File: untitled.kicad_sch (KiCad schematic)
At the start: 12 parts, among them Q1 AO3401A, U2 STM32L100RBT6A_LQFP64, U4 RC1587_3V3

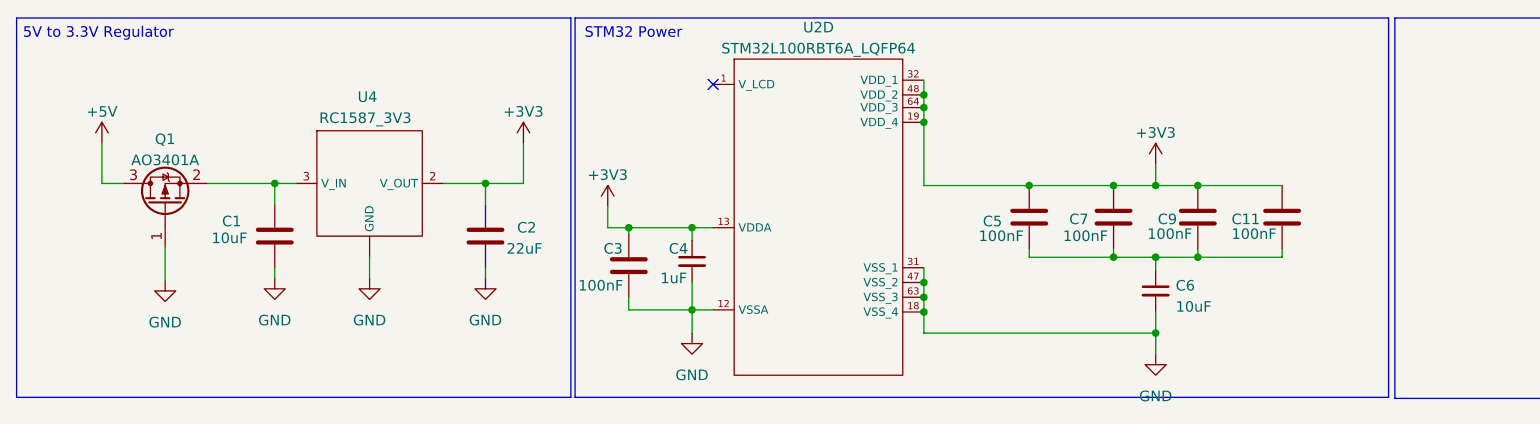
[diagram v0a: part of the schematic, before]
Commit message: Update to schem
- Updated per Adi's feedback
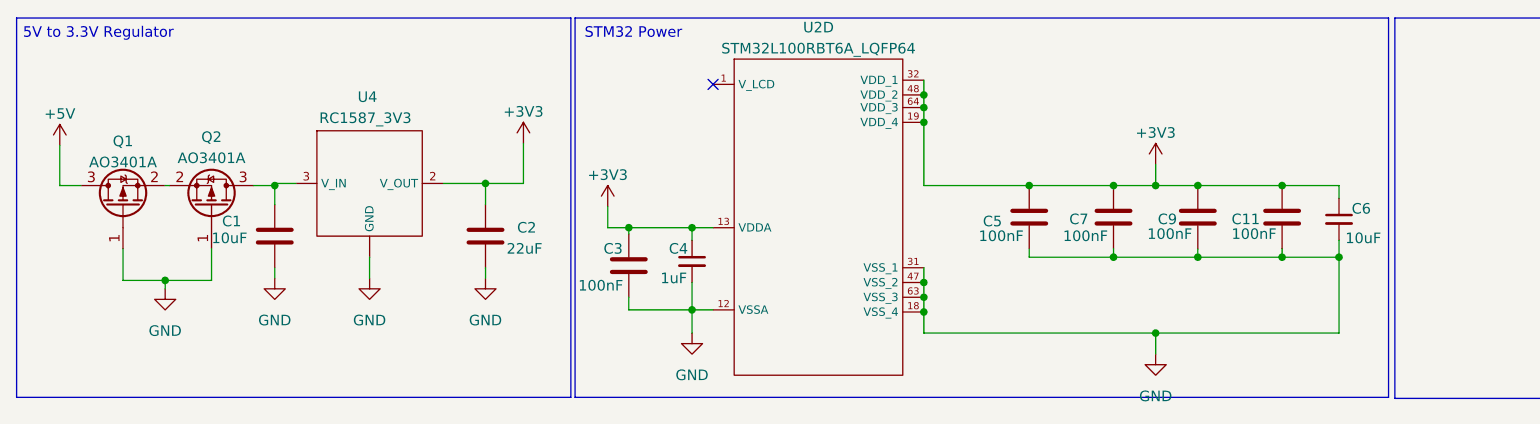
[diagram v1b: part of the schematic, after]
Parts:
- added Q2: AO3401A, Package_TO_SOT_SMD:SOT-23, symbol Transistor_FET:AO3401A
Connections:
- net +3V3: now also C6.1
- net GND: now also C11.2, C5.2, C7.2, C9.2, Q2.1 (G)
- net at C1.1, U4.3 (V_IN): now also Q2.3 (D); no longer Q1.2 (S)
- new net: Q1.2 (S), Q2.2 (S)
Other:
- moved on the sheet: C6, Q1
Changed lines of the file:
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@@
   (junction (at 121.92 25.4) (diameter 0) (color 0 0 0 0)
   )
+  (junction (at 149.86 50.8) (diameter 0) (color 0 0 0 0)
+  )
+  (junction (at 30.48 44.45) (diameter 0) (color 0 0 0 0)
+  )
   (junction (at 121.92 23.622) (diameter 0) (color 0 0 0 0)
   )
@@
   (junction (at 121.92 48.26) (diameter 0) (color 0 0 0 0)
   )
-  (junction (at 149.86 41.656) (diameter 0) (color 0 0 0 0)
-  )
   (junction (at 86.36 38.1) (diameter 0) (color 0 0 0 0)
   )
@@
   (junction (at 149.86 33.02) (diameter 0) (color 0 0 0 0)
   )
+  (junction (at 165.1 41.656) (diameter 0) (color 0 0 0 0)
+  )
   (junction (at 154.94 33.02) (diameter 0) (color 0 0 0 0)
   )
+  (junction (at 171.958 41.656) (diameter 0) (color 0 0 0 0)
+  )
   (junction (at 93.98 48.006) (diameter 0) (color 0 0 0 0)
   )
@@
   (junction (at 154.94 41.656) (diameter 0) (color 0 0 0 0)
   )
-  (junction (at 149.86 50.8) (diameter 0) (color 0 0 0 0)
-  )
-  (junction (at 43.688 32.766) (diameter 0) (color 0 0 0 0)
+  (junction (at 43.688 33.02) (diameter 0) (color 0 0 0 0)
   )
   (junction (at 144.78 33.02) (diameter 0) (color 0 0 0 0)
   )
+  (junction (at 165.1 33.02) (diameter 0) (color 0 0 0 0)
+  )
   (no_connect (at 96.52 20.828))
-  (wire (pts (xy 149.86 41.656) (xy 149.86 43.18))
-    (stroke (width 0) (type default))
-  )
   (wire (pts (xy 154.94 33.02) (xy 165.1 33.02))
     (stroke (width 0) (type default))
@@
     (stroke (width 0) (type default))
   )
-  (wire (pts (xy 30.48 40.386) (xy 30.48 44.45))
+  (wire (pts (xy 36.068 40.64) (xy 36.068 44.45))
+    (stroke (width 0) (type default))
+  )
+  (wire (pts (xy 30.48 44.45) (xy 30.48 45.466))
     (stroke (width 0) (type default))
   )
@@
     (stroke (width 0) (type default))
   )
+  (wire (pts (xy 171.958 33.02) (xy 171.958 34.544))
+    (stroke (width 0) (type default))
+  )
   (wire (pts (xy 64.008 32.766) (xy 69.088 32.766))
     (stroke (width 0) (type default))
   )
-  (wire (pts (xy 22.86 27.94) (xy 22.86 32.766))
+  (wire (pts (xy 41.148 33.02) (xy 43.688 33.02))
+    (stroke (width 0) (type default))
+  )
+  (wire (pts (xy 43.688 33.02) (xy 43.688 35.306))
+    (stroke (width 0) (type default))
+  )
+  (wire (pts (xy 17.78 28.194) (xy 17.78 33.02))
     (stroke (width 0) (type default))
   )
@@
     (stroke (width 0) (type default))
   )
-  (wire (pts (xy 35.56 32.766) (xy 43.688 32.766))
+  (wire (pts (xy 30.48 33.02) (xy 30.988 33.02))
+    (stroke (width 0) (type default))
+  )
+  (wire (pts (xy 36.068 44.45) (xy 30.48 44.45))
     (stroke (width 0) (type default))
   )
@@
     (stroke (width 0) (type default))
   )
+  (wire (pts (xy 171.958 41.656) (xy 171.958 39.624))
+    (stroke (width 0) (type default))
+  )
+  (wire (pts (xy 165.1 41.656) (xy 171.958 41.656))
+    (stroke (width 0) (type default))
+  )
   (wire (pts (xy 86.36 48.006) (xy 93.98 48.006))
     (stroke (width 0) (type default))
@@
     (stroke (width 0) (type default))
   )
-  (wire (pts (xy 149.86 48.26) (xy 149.86 50.8))
+  (wire (pts (xy 165.1 33.02) (xy 171.958 33.02))
     (stroke (width 0) (type default))
   )
@@
     (stroke (width 0) (type default))
   )
-  (wire (pts (xy 149.86 41.656) (xy 154.94 41.656))
-    (stroke (width 0) (type default))
-  )
   (wire (pts (xy 121.92 25.4) (xy 121.92 33.02))
     (stroke (width 0) (type default))
   )
+  (wire (pts (xy 25.4 44.45) (xy 25.4 40.64))
+    (stroke (width 0) (type default))
+  )
+  (wire (pts (xy 30.48 44.45) (xy 25.4 44.45))
+    (stroke (width 0) (type default))
+  )
   (wire (pts (xy 121.92 44.704) (xy 121.92 46.482))
     (stroke (width 0) (type default))
@@
     (stroke (width 0) (type default))
   )
-  (wire (pts (xy 144.78 41.656) (xy 149.86 41.656))
+  (wire (pts (xy 144.78 41.656) (xy 154.94 41.656))
     (stroke (width 0) (type default))
   )
@@
     (stroke (width 0) (type default))
   )
+  (wire (pts (xy 171.958 50.8) (xy 171.958 41.656))
+    (stroke (width 0) (type default))
+  )
   (wire (pts (xy 69.088 32.766) (xy 73.66 32.766))
     (stroke (width 0) (type default))
   )
-  (wire (pts (xy 43.688 32.766) (xy 43.688 35.306))
+  (wire (pts (xy 149.86 50.8) (xy 171.958 50.8))
     (stroke (width 0) (type default))
   )
@@
     (stroke (width 0) (type default))
   )
+  (wire (pts (xy 43.688 33.02) (xy 43.688 32.766))
+    (stroke (width 0) (type default))
+  )
   (wire (pts (xy 93.98 38.1) (xy 96.52 38.1))
     (stroke (width 0) (type default))
   )
-  (wire (pts (xy 22.86 32.766) (xy 25.4 32.766))
+  (wire (pts (xy 17.78 33.02) (xy 20.32 33.02))
     (stroke (width 0) (type default))
   )
@@
     )
   )
-  (symbol (lib_id "power:GND") (at 30.48 44.45 0) (unit 1)
-    (in_bom yes) (on_board yes) (dnp no) (fields_autoplaced)
-    (property "Reference" "#PWR029" (at 30.48 50.8 0)
-      (effects (font (size 1.27 1.27)) hide)
-    )
-    (property "Value" "GND" (at 30.48 49.53 0)
-      (effects (font (size 1.27 1.27)))
-    )
-    (property "Footprint" "" (at 30.48 44.45 0)
-      (effects (font (size 1.27 1.27)) hide)
-    )
-    (property "Datasheet" "" (at 30.48 44.45 0)
+  (symbol (lib_id "power:GND") (at 30.48 45.466 0) (unit 1)
+    (in_bom yes) (on_board yes) (dnp no) (fields_autoplaced)
+    (property "Reference" "#PWR029" (at 30.48 51.816 0)
+      (effects (font (size 1.27 1.27)) hide)
+    )
+    (property "Value" "GND" (at 30.48 50.546 0)
+      (effects (font (size 1.27 1.27)))
+    )
+    (property "Footprint" "" (at 30.48 45.466 0)
+      (effects (font (size 1.27 1.27)) hide)
+    )
+    (property "Datasheet" "" (at 30.48 45.466 0)
       (effects (font (size 1.27 1.27)) hide)
     )
@@
     )
   )
-  (symbol (lib_id "Transistor_FET:AO3401A") (at 30.48 35.306 90) (unit 1)
-    (in_bom yes) (on_board yes) (dnp no) (fields_autoplaced)
-    (property "Reference" "Q1" (at 30.48 27.432 90)
-      (effects (font (size 1.27 1.27)))
-    )
-    (property "Value" "AO3401A" (at 30.48 29.972 90)
-      (effects (font (size 1.27 1.27)))
-    )
-    (property "Footprint" "Package_TO_SOT_SMD:SOT-23" (at 32.385 30.226 0)
+  (symbol (lib_id "Transistor_FET:AO3401A") (at 25.4 35.56 90) (unit 1)
+    (in_bom yes) (on_board yes) (dnp no) (fields_autoplaced)
+    (property "Reference" "Q1" (at 25.4 27.686 90)
+      (effects (font (size 1.27 1.27)))
+    )
+    (property "Value" "AO3401A" (at 25.4 30.226 90)
+      (effects (font (size 1.27 1.27)))
+    )
+    (property "Footprint" "Package_TO_SOT_SMD:SOT-23" (at 27.305 30.48 0)
       (effects (font (size 1.27 1.27) italic) (justify left) hide)
     )
-    (property "Datasheet" "http://www.aosmd.com/pdfs/datasheet/AO3401A.pdf" (at 30.48 35.306 0)
+    (property "Datasheet" "http://www.aosmd.com/pdfs/datasheet/AO3401A.pdf" (at 25.4 35.56 0)
       (effects (font (size 1.27 1.27)) (justify left) hide)
     )
@@
     )
   )
-  (symbol (lib_id "Device:C_Small") (at 149.86 45.72 0) (unit 1)
-    (in_bom yes) (on_board yes) (dnp no) (fields_autoplaced)
-    (property "Reference" "C6" (at 152.273 45.0913 0)
-      (effects (font (size 1.27 1.27)) (justify left))
-    )
-    (property "Value" "10uF" (at 152.273 47.6313 0)
-      (effects (font (size 1.27 1.27)) (justify left))
-    )
-    (property "Footprint" "Capacitor_SMD:C_0805_2012Metric" (at 149.86 45.72 0)
-      (effects (font (size 1.27 1.27)) hide)
-    )
-    (property "Datasheet" "~" (at 149.86 45.72 0)
+  (symbol (lib_id "Transistor_FET:AO3401A") (at 36.068 35.56 270) (mirror x) (unit 1)
+    (in_bom yes) (on_board yes) (dnp no)
+    (property "Reference" "Q2" (at 36.068 27.178 90)
+      (effects (font (size 1.27 1.27)))
+    )
+    (property "Value" "AO3401A" (at 36.068 29.718 90)
+      (effects (font (size 1.27 1.27)))
+    )
+    (property "Footprint" "Package_TO_SOT_SMD:SOT-23" (at 34.163 30.48 0)
+      (effects (font (size 1.27 1.27) italic) (justify left) hide)
+    )
+    (property "Datasheet" "http://www.aosmd.com/pdfs/datasheet/AO3401A.pdf" (at 36.068 35.56 0)
+      (effects (font (size 1.27 1.27)) (justify left) hide)
+    )
+    (pin "1")
+    (pin "2")
+    (pin "3")
+    (instances
+      (project "Sensor Hub"
+        (path "/c4cdbb0f-2866-4a3f-8578-00adb185b068/8fa77c20-106e-495a-881a-4ce54bf79ad5"
+          (reference "Q2") (unit 1)
+        )
+      )
+    )
+  )
+  (symbol (lib_id "Device:C_Small") (at 171.958 37.084 0) (unit 1)
+    (in_bom yes) (on_board yes) (dnp no)
+    (property "Reference" "C6" (at 173.482 35.814 0)
+      (effects (font (size 1.27 1.27)) (justify left))
+    )
+    (property "Value" "10uF" (at 172.72 39.37 0)
+      (effects (font (size 1.27 1.27)) (justify left))
+    )
+    (property "Footprint" "Capacitor_SMD:C_0805_2012Metric" (at 171.958 37.084 0)
+      (effects (font (size 1.27 1.27)) hide)
+    )
+    (property "Datasheet" "~" (at 171.958 37.084 0)
       (effects (font (size 1.27 1.27)) hide)
     )
@@
     )
   )
-  (symbol (lib_id "power:+5V") (at 22.86 27.94 0) (unit 1)
-    (in_bom yes) (on_board yes) (dnp no) (fields_autoplaced)
-    (property "Reference" "#PWR05" (at 22.86 31.75 0)
-      (effects (font (size 1.27 1.27)) hide)
-    )
-    (property "Value" "+5V" (at 22.86 24.13 0)
-      (effects (font (size 1.27 1.27)))
-    )
-    (property "Footprint" "" (at 22.86 27.94 0)
-      (effects (font (size 1.27 1.27)) hide)
-    )
-    (property "Datasheet" "" (at 22.86 27.94 0)
-      (effects (font (size 1.27 1.27)) hide)
-    )
+  (symbol (lib_id "power:+5V") (at 17.78 28.194 0) (unit 1)
+    (in_bom yes) (on_board yes) (dnp no) (fields_autoplaced)
+    (property "Reference" "#PWR05" (at 17.78 32.004 0)
+      (effects (font (size 1.27 1.27)) hide)
+    )
+    (property "Value" "+5V" (at 17.78 24.384 0)
+      (effects (font (size 1.27 1.27)))
+    )
+    (property "Footprint" "" (at 17.78 28.194 0)
+      (effects (font (size 1.27 1.27)) hide)
+    )
+    (property "Datasheet" "" (at 17.78 28.194 0)
+      (effects (font (size 1.27 1.27)) hide)
+    )

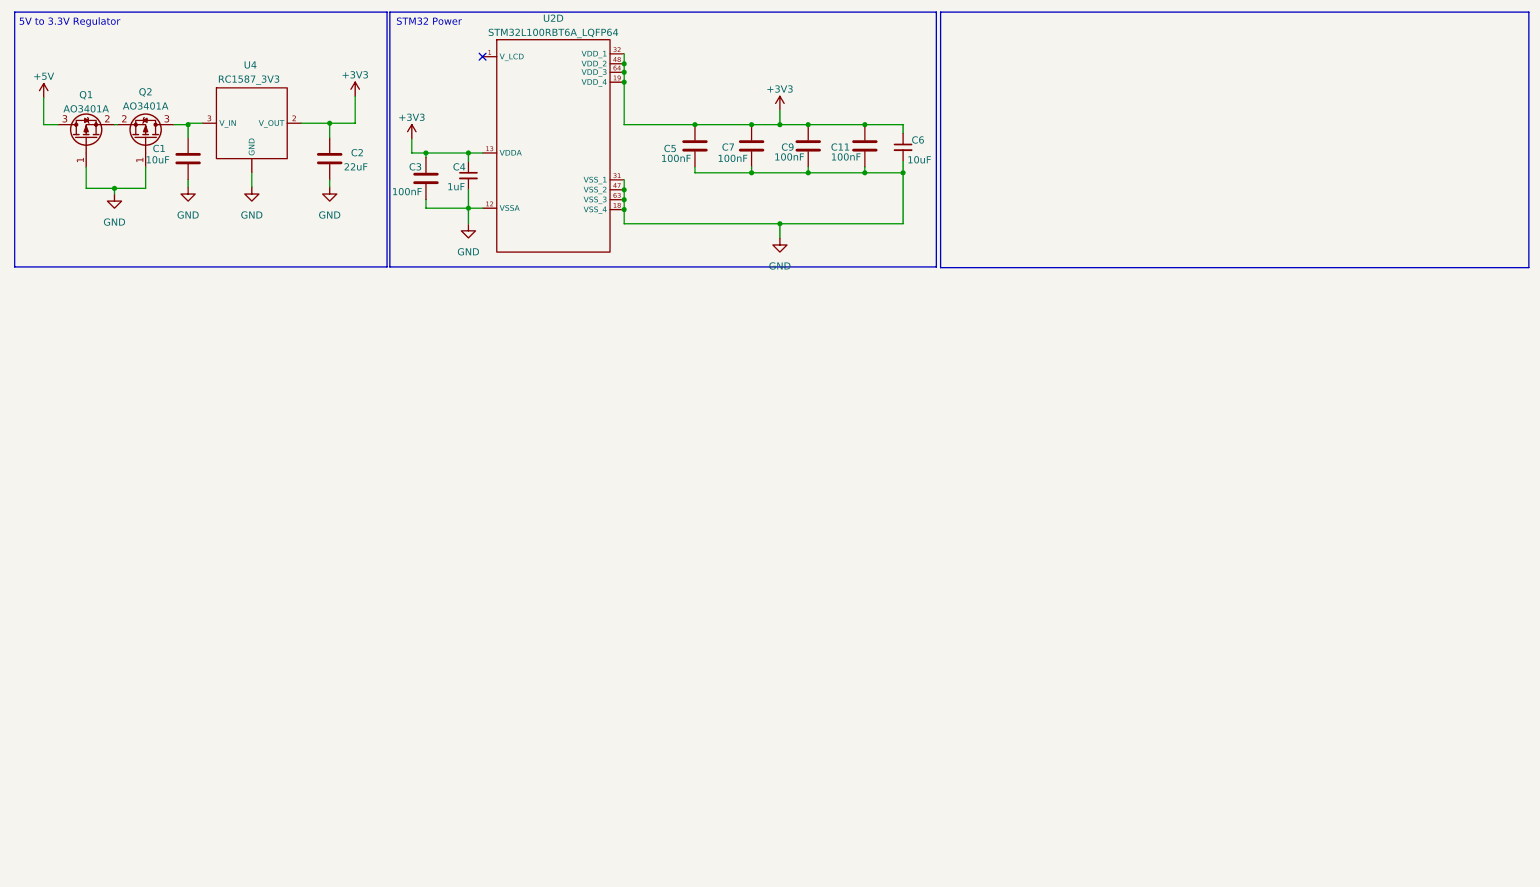
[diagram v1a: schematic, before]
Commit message: Updated Schematic
- Added LTC4002 battery management IC
- Updated previous ICs to reflect given feedback
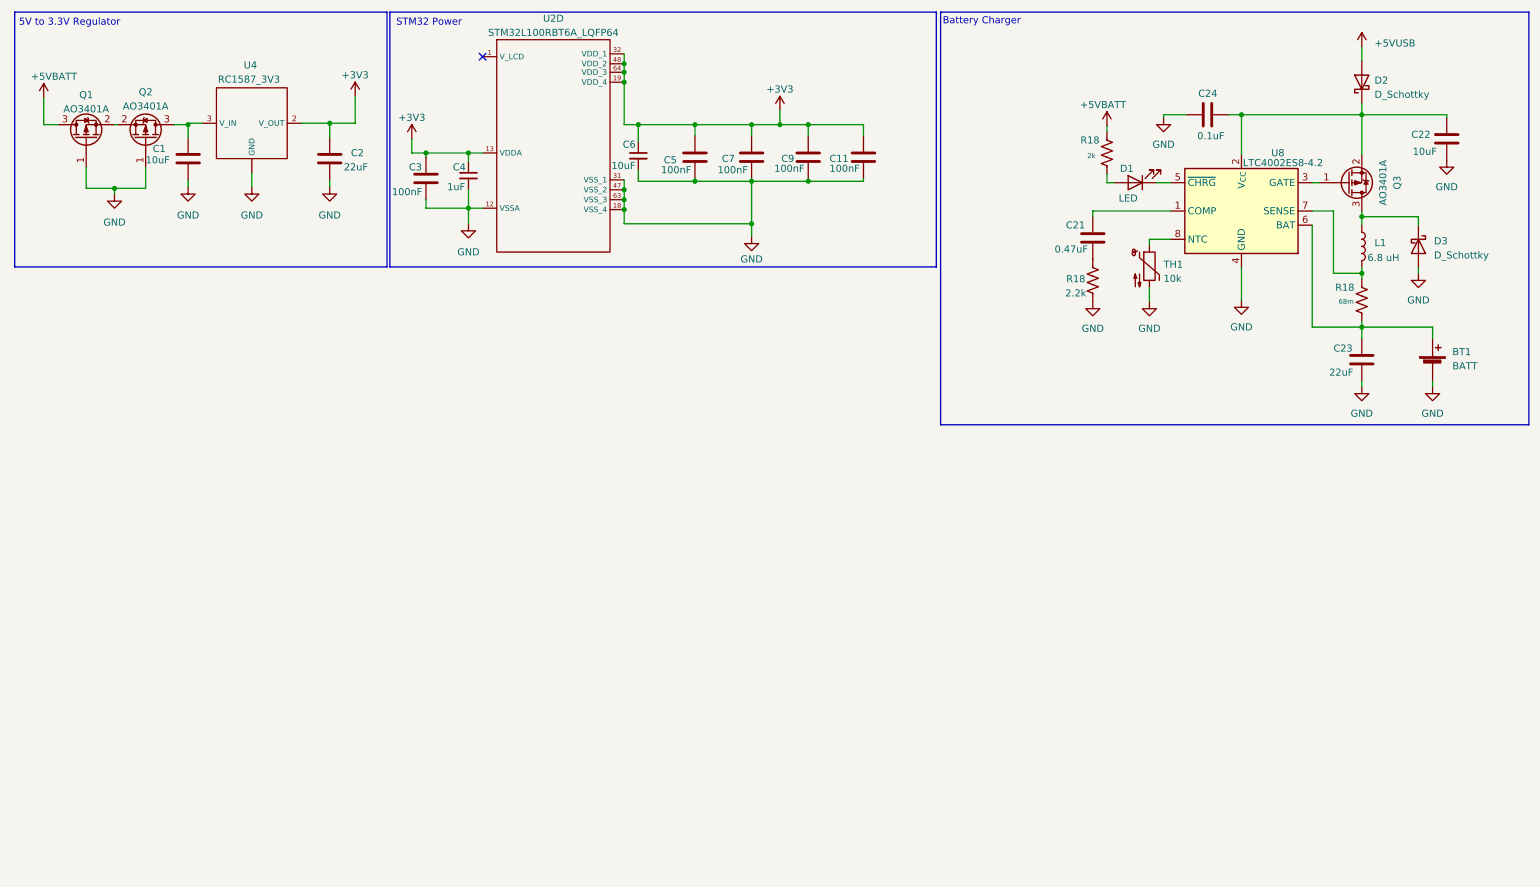
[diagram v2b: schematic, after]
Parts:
- added BT1: BATT, symbol Device:Battery_Cell
- added C21: 0.47uF, Capacitor_SMD:C_0805_2012Metric, symbol Device:C
- added C22: 10uF, Capacitor_SMD:C_0805_2012Metric, symbol Device:C
- added C23: 22uF, Capacitor_SMD:C_0805_2012Metric, symbol Device:C
- added C24: 0.1uF, Capacitor_SMD:C_0805_2012Metric, symbol Device:C
- added D1: LED, symbol Device:LED
- added D2, D3: D_Schottky, symbol Device:D_Schottky
- added L1: 6.8 uH, symbol Device:L
- added Q3: AO3401A, Package_TO_SOT_SMD:SOT-23, symbol Transistor_FET:AO3401A
- added R18: 2k, Resistor_SMD:R_0805_2012Metric, symbol Device:R_US
- added R18: 2.2k, Resistor_SMD:R_0805_2012Metric, symbol Device:R_US
- added R18: 68m, Resistor_SMD:R_0805_2012Metric, symbol Device:R_US
- added TH1: 10k, symbol Device:Thermistor_NTC
- added U8: LTC4002ES8-4.2, Package_SO:SOIC-8_3.9x4.9mm_P1.27mm, symbol Battery_Management:LTC4002ES8-4.2
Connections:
- net +5V: now also D2.2 (A)
- net GND: now also BT1.2 (-), C22.2, C23.2, C24.1, D3.2 (A), R18.1, TH1.2, U8.4 (GND)
- new net: C22.1, C24.2, D2.1 (K), Q3.2 (S), U8.2 (V_{CC})
- new net: BT1.1 (+), C23.1, R18.1, U8.6 (BAT)
- new net: D3.1 (K), L1.1, Q3.3 (D)
- new net: C21.1, U8.1 (COMP)
- new net: C21.2, R18.2
- new net: TH1.1, U8.8 (NTC)
- new net: D1.2 (A), R18.1
- new net: L1.2, R18.2, U8.7 (SENSE)
- new net: Q3.1 (G), U8.3 (GATE)
- new net: D1.1 (K), U8.5 (~{CHRG})
- new net +BATT: R18.2
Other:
- note added: "Battery Charger"
- moved on the sheet: C11, C5, C7, C9
